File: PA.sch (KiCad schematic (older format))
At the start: 0 parts

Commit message: Added CC1190 library
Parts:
- added U4: CC1190RGVR, QFN65P400X400X100-17N, symbol CC1190RGVR:CC1190RGVR
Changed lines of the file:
@@
 $Descr A4 11693 8268
 encoding utf-8
-Sheet 1 6
+Sheet 5 6
 Title ""
 Date ""
@@
 Comment4 ""
 $EndDescr
+$Comp
+L CC1190RGVR:CC1190RGVR U4
+U 1 1 60188BB7
+P 5650 3450
+F 0 "U4" H 5650 4720 50  0000 C CNN
+F 1 "CC1190RGVR" H 5650 4629 50  0000 C CNN
+F 2 "QFN65P400X400X100-17N" H 5650 3450 50  0001 L BNN
+F 3 "" H 5650 3450 50  0001 L BNN
+	1    5650 3450
+	1    0    0    -1
+$EndComp
 $EndSCHEMATC

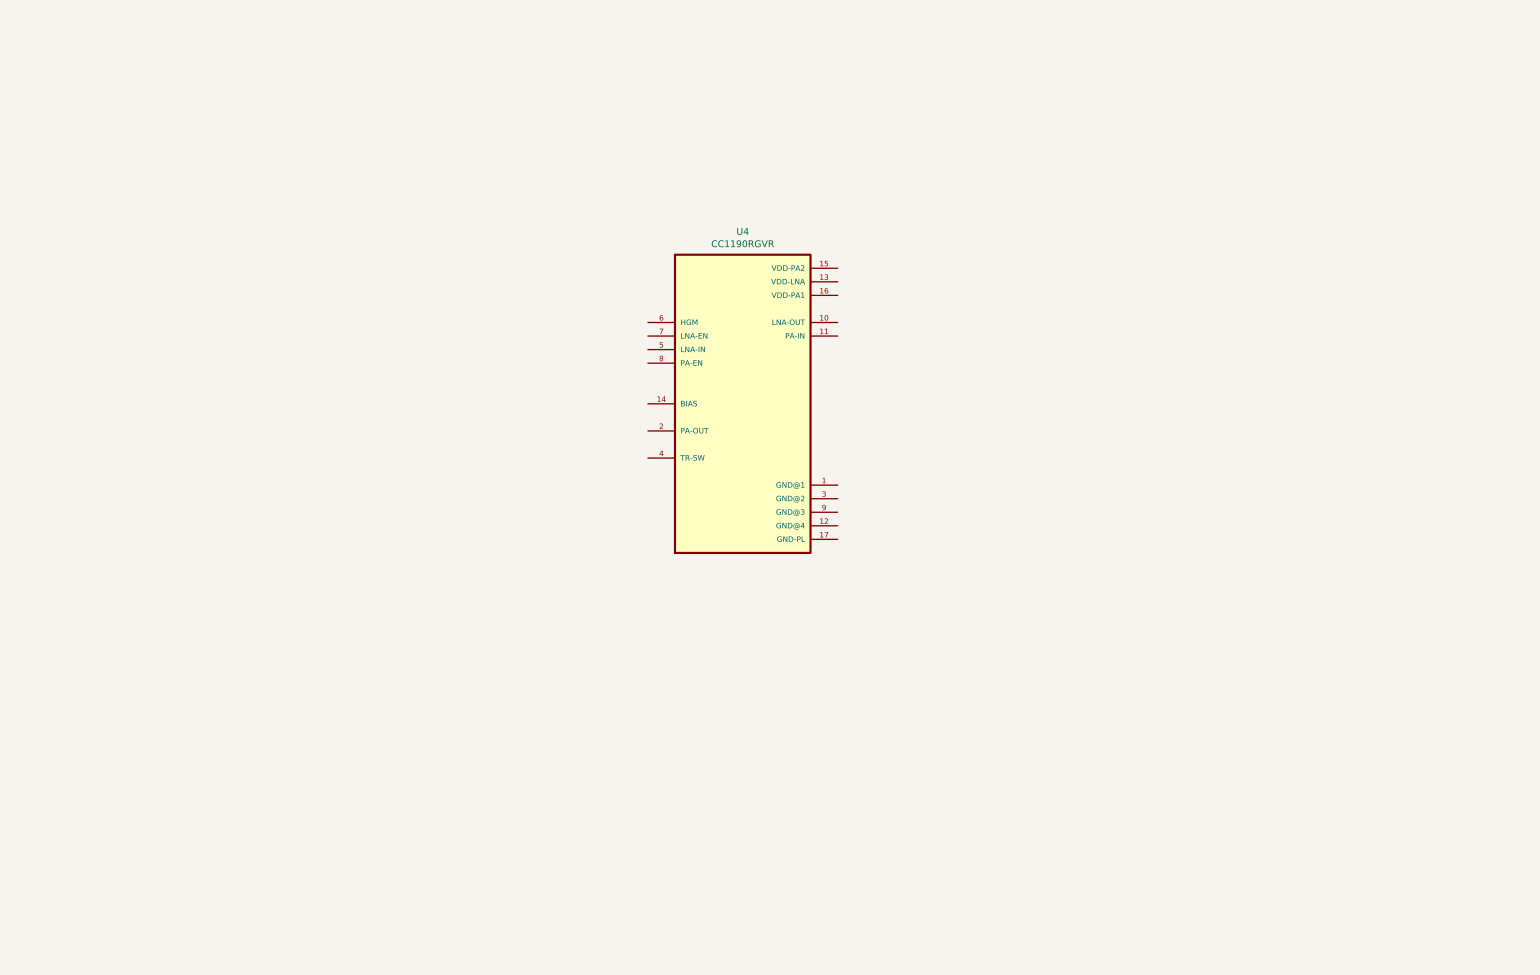
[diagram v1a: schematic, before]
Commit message: Added cc1190 reference design
also changed cc1190 symbol
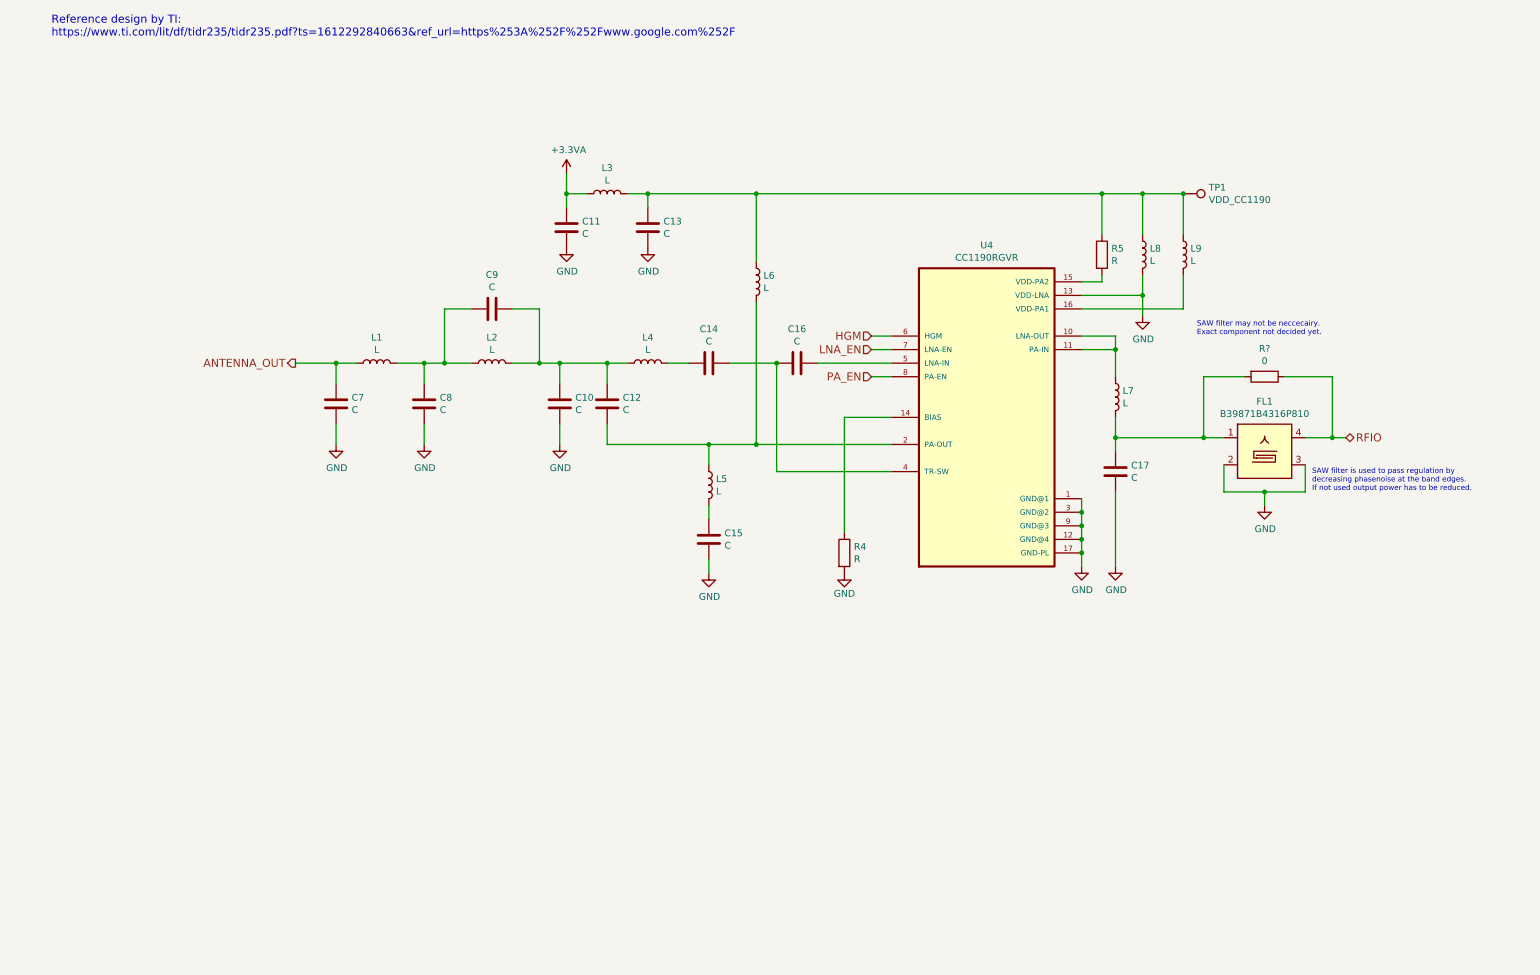
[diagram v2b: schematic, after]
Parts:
- added C10, C11, C12, C13, C14, C15, C16, C17, C7, C8, C9: C, symbol Device:C
- added FL1: B39871B4316P810, Filter:Filter_1109-5_1.1x0.9mm, symbol Filter:B39162B8813P810
- added L1, L2, L3, L4, L5, L6, L7, L8, L9: L, symbol Device:L
- added R4, R5: R, symbol Device:R
- added R?: 0, symbol Device:R
- added TP1: VDD_CC1190, symbol Connector:TestPoint
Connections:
- net GND: now reaches U4.1 (GND@1)
- net GND: now also U4.12 (GND@4), U4.13 (VDD-LNA), U4.17 (GND-PL), U4.3 (GND@2), U4.9 (GND@3), C10.2, C11.2, C13.2, C15.2, C17.2, C7.2, C8.2, FL1.2, FL1.3, FL1.5, L8.2, R4.2
- net at U4.10 (LNA-OUT): now also U4.11 (PA-IN), L7.1
- net at U4.14 (BIAS): now also R4.1
- net at U4.15 (VDD-PA2): now also R5.2
- net at U4.16 (VDD-PA1): now also L9.2
- net at U4.2 (PA-OUT): now also C12.2, L5.1, L6.2
- net at U4.4 (TR-SW): now also C14.1, C16.2
- net at U4.5 (LNA-IN): now also C16.1
- net HGM: now reaches U4.6 (HGM)
- net LNA_EN: now reaches U4.7 (LNA-EN)
- net PA_EN: now reaches U4.8 (PA-EN)
- new net: C13.1, L3.2, L6.1, L8.1, L9.1, R5.1, TP1.1
- new net: C15.1, L5.2
- new net: C14.2, L4.2
- new net: C10.1, C12.1, C9.1, L2.2, L4.1
- new net: C17.1, FL1.1, L7.2, R?.2
- new net: C8.1, C9.2, L1.2, L2.1
- new net +3.3VA: C11.1, L3.1
- new net ANTENNA_OUT: C7.1, L1.1
- new net RFIO: FL1.4, R?.1
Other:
- note added: "Reference design by TI:\nhttps://www.ti.com/lit/df/tidr235/tidr235.pdf?ts=1612292840663&ref_url=https%253A%252F%252Fwww.google.com%252F"
- note added: "SAW filter is used to pass regulation by\ndecreasing phasenoise at the band edges.\nIf not used output power has to be reduced."
- note added: "SAW filter may not be neccecairy. \nExact component not decided yet."
- moved on the sheet: U4

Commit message: Started work on CC1200
might not be actual final tranciever
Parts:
- gave numbers to parts that had none: 1
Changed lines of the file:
@@
 $EndComp
 $Comp
-L Device:R R?
+L Device:R R7
 U 1 1 60230E08
 P 9500 3250
-F 0 "R?" V 9293 3250 50  0000 C CNN
+F 0 "R7" V 9293 3250 50  0000 C CNN
 F 1 "0" V 9384 3250 50  0000 C CNN
 F 2 "" V 9430 3250 50  0001 C CNN

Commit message: More work on tranciever and PA
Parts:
- added J6: RF_Shield_One_Piece, symbol Device:RF_Shield_One_Piece
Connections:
- net GND: now also J6.1 (Shield)
- net +3.3VA renamed +3V3
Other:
- moved on the sheet: C10, C11, C12, C13, C14, C15, C16, C17, C7, C8, C9, FL1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

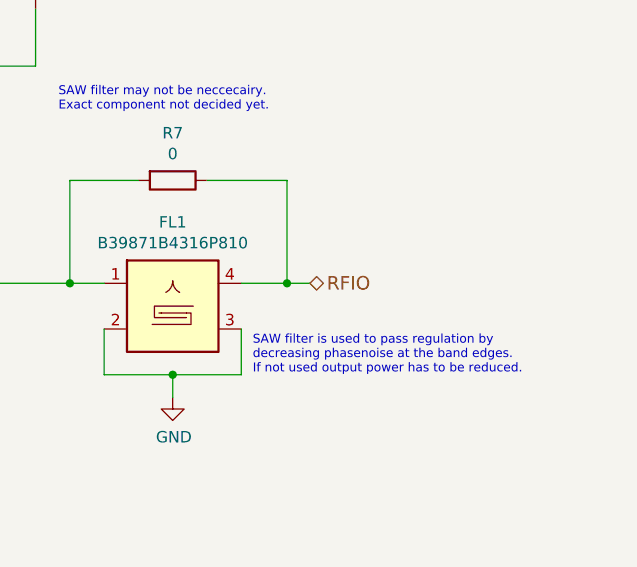
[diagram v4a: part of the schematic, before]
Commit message: Added mount for RFM98/95
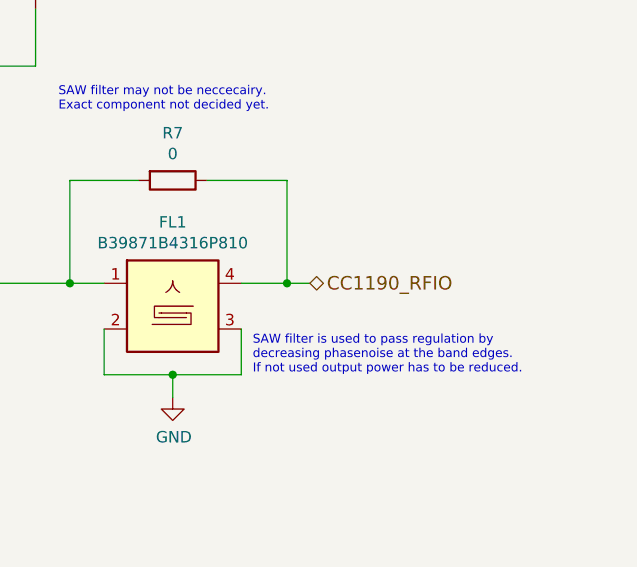
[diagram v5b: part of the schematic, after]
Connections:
- net RFIO renamed CC1190_RFIO
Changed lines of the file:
@@
 $EndComp
 Text HLabel 9550 3600 2    59   BiDi ~ 0
-RFIO
+CC1190_RFIO
 $Comp
 L power:GND #PWR013

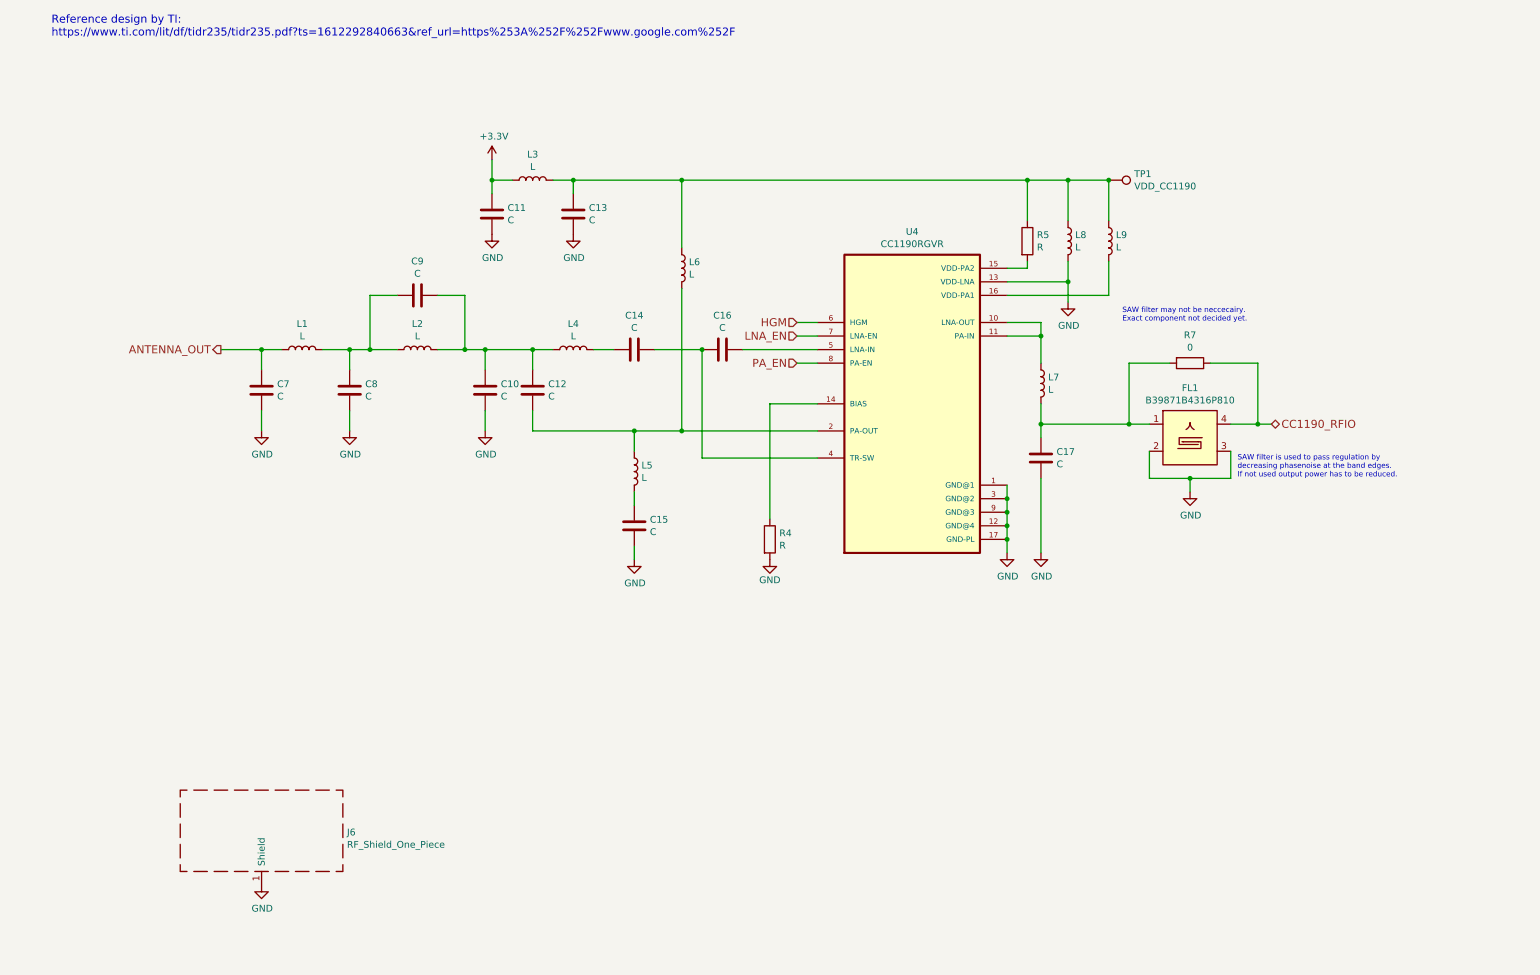
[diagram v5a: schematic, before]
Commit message: Added component values for tranciever and PA
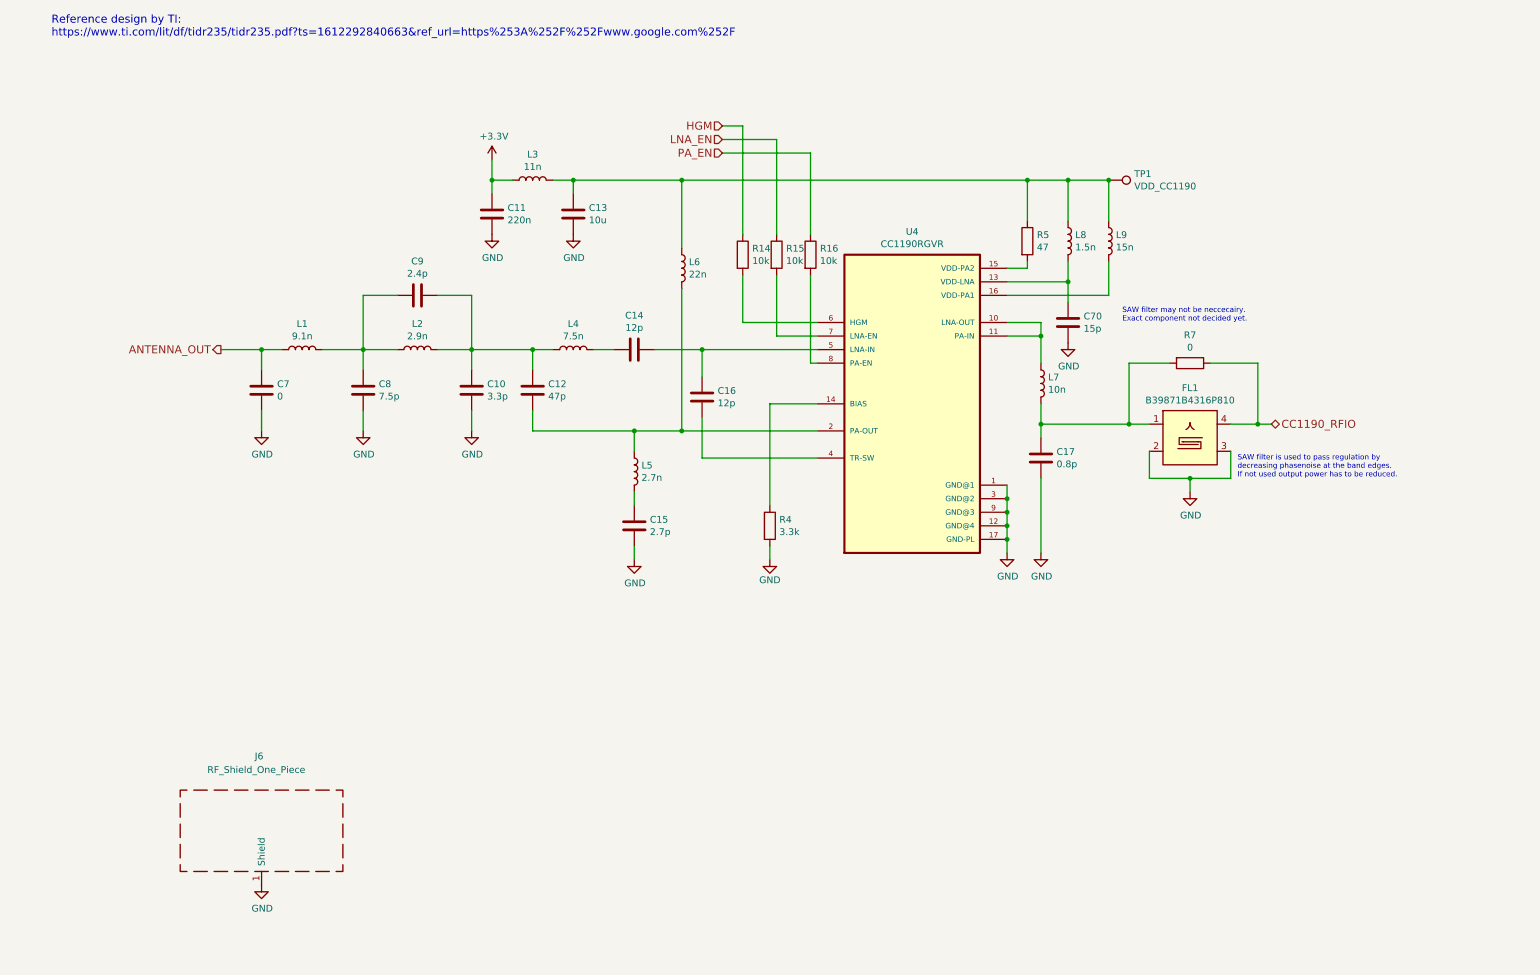
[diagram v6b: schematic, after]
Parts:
- added C70: 15p, symbol Device:C
- added R14, R15, R16: 10k, symbol Device:R
- C10: value C -> 3.3p
- C11: value C -> 220n
- C12: value C -> 47p
- C13: value C -> 10u
- C14, C16: value C -> 12p
- C15: value C -> 2.7p
- C17: value C -> 0.8p
- C7: value C -> 0
- C8: value C -> 7.5p
- C9: value C -> 2.4p
- L1: value L -> 9.1n
- L2: value L -> 2.9n
- L3: value L -> 11n
- L4: value L -> 7.5n
- L5: value L -> 2.7n
- L6: value L -> 22n
- L7: value L -> 10n
- L8: value L -> 1.5n
- L9: value L -> 15n
- R4: value R -> 3.3k
- R5: value R -> 47
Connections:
- net GND: now also C70.2; no longer L8.2, U4.13 (VDD-LNA)
- net HGM: now also R14.1; no longer U4.6 (HGM)
- net LNA_EN: now also R15.1; no longer U4.7 (LNA-EN)
- net PA_EN: now also R16.1; no longer U4.8 (PA-EN)
- net at C16.2, U4.4 (TR-SW): no longer C14.1
- net at C16.1, U4.5 (LNA-IN): now also C14.1
- new net: C70.1, L8.2, U4.13 (VDD-LNA)
- new net: R14.2, U4.6 (HGM)
- new net: R15.2, U4.7 (LNA-EN)
- new net: R16.2, U4.8 (PA-EN)
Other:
- moved on the sheet: C10, C8, R4
